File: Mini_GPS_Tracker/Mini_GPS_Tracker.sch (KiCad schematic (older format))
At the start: 0 parts

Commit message: Add files via upload
Breaking out more pins
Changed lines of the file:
@@
 F2 "SCL" I R 10450 2100 50
 F3 "SDA" I R 10450 2200 50
-F4 "9_SDA" I R 10450 2300 50
-F5 "9_SCL" I R 10450 2400 50
-F6 "accel_cs" I L 9000 2000 50
-F7 "accel_scl" I L 9000 2100 50
-F8 "accel_sda" I L 9000 2200 50
-F9 "accel_sdo" I L 9000 2300 50
-F10 "BNO055_SCL" I L 9000 2400 50
-F11 "BNO055_SDA" I L 9000 2500 50
-F12 "BNO055_RESET" I L 9000 2600 50
-F13 "BNO055_INTERRUPT" I L 9000 2700 50
+F4 "accel_cs" I L 9000 2000 50
+F5 "accel_scl" I L 9000 2100 50
+F6 "accel_sda" I L 9000 2200 50
+F7 "accel_sdo" I L 9000 2300 50
+F8 "BNO055_SCL" I L 9000 2400 50
+F9 "BNO055_SDA" I L 9000 2500 50
+F10 "BNO055_RESET" I L 9000 2600 50
+F11 "BNO055_INTERRUPT" I L 9000 2700 50
 $EndSheet
 Wire Wire Line
@@
 F2 "TX" I R 10400 4950 50
 F3 "RX" I R 10400 5050 50
-F4 "murata_tx" I L 9050 4900 50
-F5 "murata_rx" I L 9050 5000 50
-F6 "murata_rts" I L 9050 5100 50
-F7 "murata_cts" I L 9050 5200 50
 $EndSheet
 Text GLabel 10600 3500 2    50   Input ~ 0
@@
 F0 "IO" 50
 F1 "IO.sch" 50
+F2 "RESET" I L 9350 1050 50
+F3 "SWDCK" I L 9350 1150 50
+F4 "SWDIO" I L 9350 1250 50
+F5 "SWO" I L 9350 1350 50
+F6 "QWIIC_SCL" I L 9350 1450 50
+F7 "QWIIC_SDA" I L 9350 1550 50
+F8 "RTS" I L 9350 1650 50
 $EndSheet
 $Sheet
@@
 F0 "USB" 50
 F1 "USB.sch" 50
+F2 "USB_TX" I L 7300 3300 50
+F3 "USB_RX" I L 7300 3400 50
+F4 "RTS" I L 7300 3500 50
+F5 "VBUS" I L 7300 3600 50
 $EndSheet
 $Sheet
@@
 F0 "Siren LED Flashe" 50
 F1 "Siren LED Flasher.sch" 50
+F2 "Siren_on" I L 7550 1950 50
+F3 "LED_Flasher_on" I L 7550 1850 50
 $EndSheet
 $Sheet
@@
 F0 "WiFi-BT" 50
 F1 "WiFi-BT.sch" 50
+F2 "BT_WIFI_TX" I L 5200 5300 50
+F3 "BT_WIFI_RX" I L 5200 5450 50
+F4 "BT_WIFI_RTS" I L 5200 5600 50
+F5 "BT_WIFI_CTS" I L 5200 5700 50
 $EndSheet
 $EndSCHEMATC

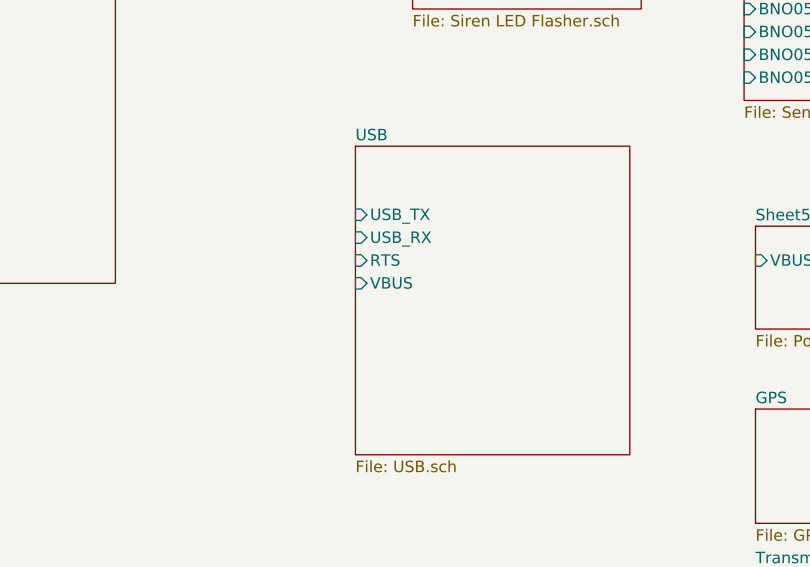
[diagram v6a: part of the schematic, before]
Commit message: Add files via upload
More changes - USB, WiFi/BT, Buzzer, Siren-LED Flasher
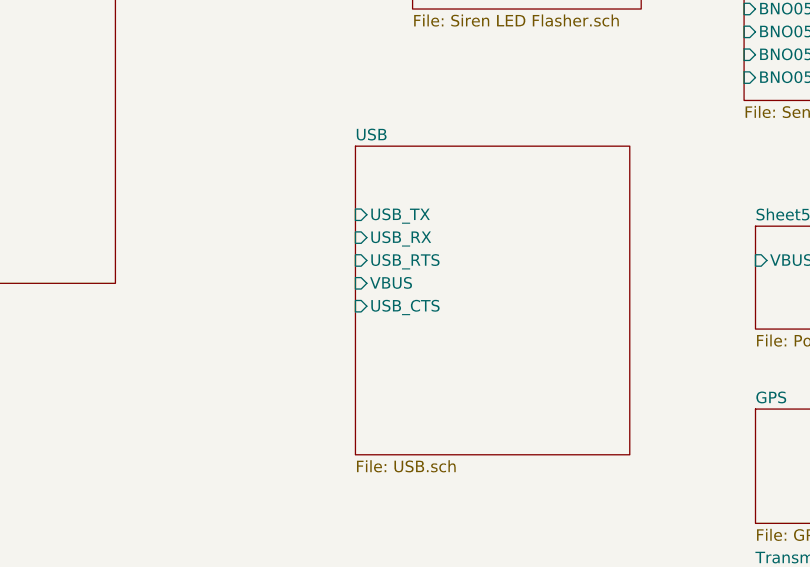
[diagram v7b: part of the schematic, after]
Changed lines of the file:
@@
 F2 "USB_TX" I L 7300 3300 50
 F3 "USB_RX" I L 7300 3400 50
-F4 "RTS" I L 7300 3500 50
-F5 "VBUS" I L 7300 3600 50
+F4 "VBUS" I L 7300 3600 50
+F5 "USB_RTS" I L 7300 3500 50
+F6 "USB_CTS" I L 7300 3700 50
 $EndSheet
 $Sheet

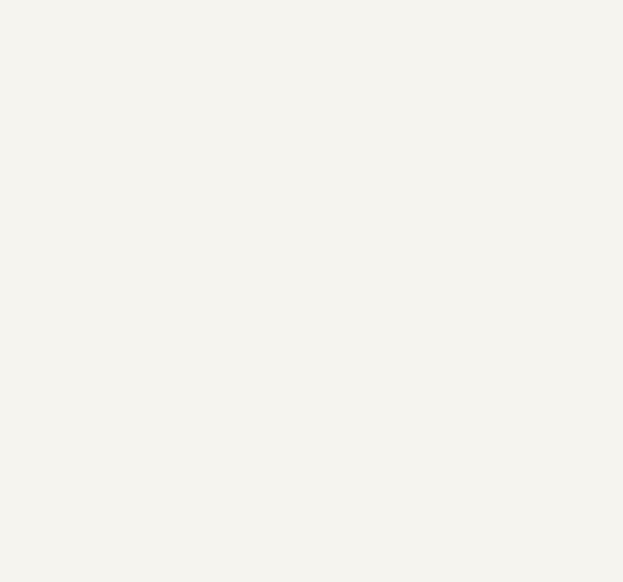
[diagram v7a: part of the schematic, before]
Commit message: Add files via upload
Added RFM95 board
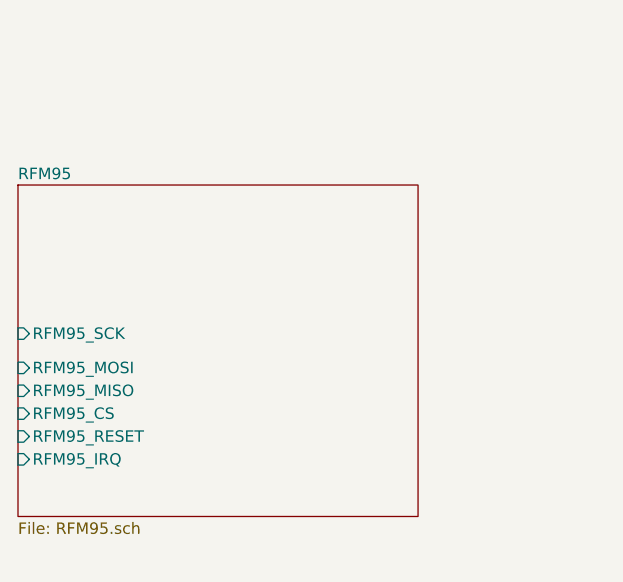
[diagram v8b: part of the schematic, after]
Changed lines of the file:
@@
 $Descr A4 11693 8268
 encoding utf-8
-Sheet 1 13
+Sheet 1 14
 Title ""
 Date ""
@@
 F5 "BT_WIFI_CTS" I L 5200 5700 50
 $EndSheet
+$Sheet
+S 2300 4750 1750 1450
+U 5EBC1C4A
+F0 "RFM95" 50
+F1 "RFM95.sch" 50
+F2 "RFM95_SCK" I L 2300 5400 50
+F3 "RFM95_MOSI" I L 2300 5550 50
+F4 "RFM95_MISO" I L 2300 5650 50
+F5 "RFM95_CS" I L 2300 5750 50
+F6 "RFM95_RESET" I L 2300 5850 50
+F7 "RFM95_IRQ" I L 2300 5950 50
+$EndSheet
 $EndSCHEMATC
